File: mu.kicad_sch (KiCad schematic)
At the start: 69 parts, among them J1 JTAG-10 PIN, J4 2060-1452/998-404, J5 ESQ-110-X-X-D, U1 STM32F042F6P6, U10 TLV3603QDCKRQ1, U11 SN74LVC1G74DCUT, U12 LM4040AIM3-2.5/NOPB, U13 MCP4921-E/SN, U14 BMP390, U2 MAX5026EUT_T, U3 MICROFC-60035-SMT-TR1, U4 TLV70433DBVT, U5 W25Q128JVS, U6 OPA656NB/250, U8 LT3045xDD, U9 sn65hvd230

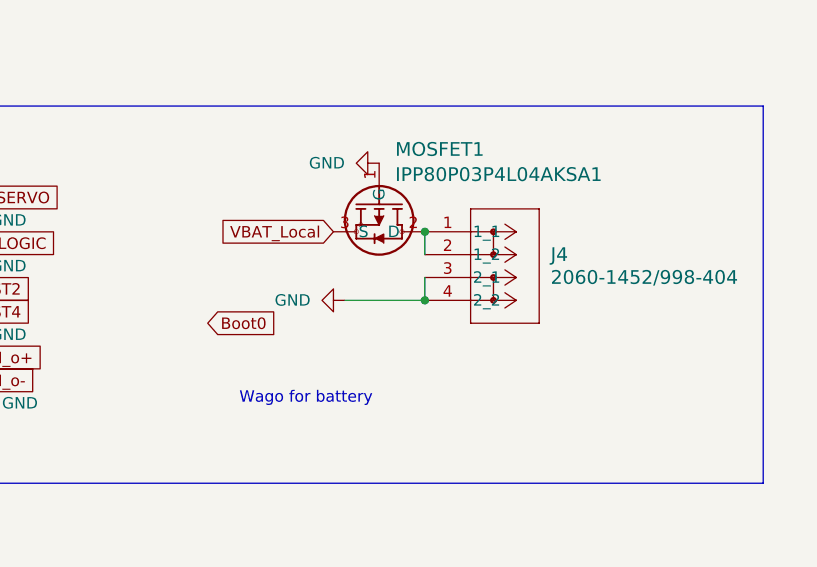
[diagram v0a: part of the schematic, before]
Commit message: xt30 added
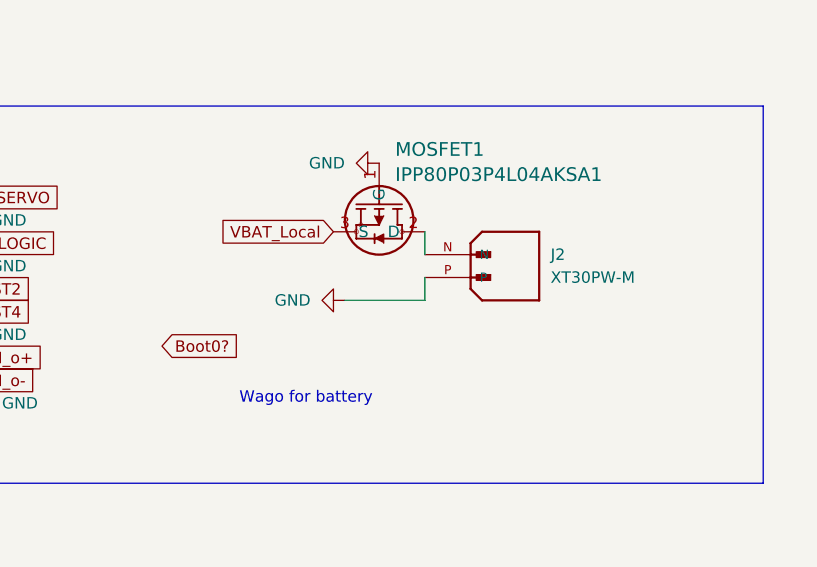
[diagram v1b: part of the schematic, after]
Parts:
- removed J4: 2060-1452/998-404, footprints:WAG, symbol Wago_2060-1452 998-404:2060-1452_998-404
- added J2: XT30PW-M, AMASS_XT30PW-M, symbol XT30PW-M:XT30PW-M
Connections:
- net GND: now also J2.P
- net at MOSFET1.2 (D): now also J2.N
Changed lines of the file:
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@@
 	)
 	(junction
-		(at 361.95 176.53)
-		(diameter 0)
-		(color 0 0 0 0)
-	)
-	(junction
 		(at 256.54 110.49)
 		(diameter 0)
@@
 	)
 	(junction
-		(at 361.95 184.15)
-		(diameter 0)
-		(color 0 0 0 0)
-	)
-	(junction
 		(at 213.36 215.9)
 		(diameter 0)
@@
 		)
 	)
-	(global_label "Boot0"
+	(global_label "Boot0?"
 		(shape input)
-		(at 337.82 186.69 0)
+		(at 332.74 189.23 0)
 		(fields_autoplaced yes)
 		(effects
@@
 		)
 		(property "Intersheetrefs" "${INTERSHEET_REFS}"
-			(at 346.3084 186.69 0)
+			(at 342.317 189.23 0)
 			(effects
 				(font
@@
 	)
 	(symbol
+		(lib_id "XT30PW-M:XT30PW-M")
+		(at 367.03 181.61 180)
+		(unit 1)
+		(exclude_from_sim no)
+		(in_bom yes)
+		(on_board yes)
+		(dnp no)
+		(fields_autoplaced yes)
+		(property "Reference" "J2"
+			(at 375.92 179.0699 0)
+			(effects
+				(font
+					(size 1.27 1.27)
+				)
+				(justify right)
+			)
+		)
+		(property "Value" "XT30PW-M"
+			(at 375.92 181.6099 0)
+			(effects
+				(font
+					(size 1.27 1.27)
+				)
+				(justify right)
+			)
+		)
+		(property "Footprint" "AMASS_XT30PW-M"
+			(at 367.03 181.61 0)
+			(effects
+				(font
+					(size 1.27 1.27)
+				)
+				(justify bottom)
+				(hide yes)
+			)
+		)
+		(property "Datasheet" ""
+			(at 367.03 181.61 0)
+			(effects
+				(font
+					(size 1.27 1.27)
+				)
+				(hide yes)
+			)
+		)
+		(property "Description" ""
+			(at 367.03 181.61 0)
+			(effects
+				(font
+					(size 1.27 1.27)
+				)
+				(hide yes)
+			)
+		)
+		(property "MF" "AMASS"
+			(at 367.03 181.61 0)
+			(effects
+				(font
+					(size 1.27 1.27)
+				)
+				(justify bottom)
+				(hide yes)
+			)
+		)
+		(property "MAXIMUM_PACKAGE_HEIGHT" "5 mm"
+			(at 367.03 181.61 0)
+			(effects
+				(font
+					(size 1.27 1.27)
+				)
+				(justify bottom)
+				(hide yes)
+			)
+		)
+		(property "Package" "None"
+			(at 367.03 181.61 0)
+			(effects
+				(font
+					(size 1.27 1.27)
+				)
+				(justify bottom)
+				(hide yes)
+			)
+		)
+		(property "Price" "None"
+			(at 367.03 181.61 0)
+			(effects
+				(font
+					(size 1.27 1.27)
+				)
+				(justify bottom)
+				(hide yes)
+			)
+		)
+		(property "Check_prices" "https://www.snapeda.com/parts/XT30PW-M/AMASS/view-part/?ref=eda"
+			(at 367.03 181.61 0)
+			(effects
+				(font
+					(size 1.27 1.27)
+				)
+				(justify bottom)
+				(hide yes)
+			)
+		)
+		(property "STANDARD" "Manufacturer Recommendations"
+			(at 367.03 181.61 0)
+			(effects
+				(font
+					(size 1.27 1.27)
+				)
+				(justify bottom)
+				(hide yes)
+			)
+		)
+		(property "PARTREV" "1.2"
+			(at 367.03 181.61 0)
+			(effects
+				(font
+					(size 1.27 1.27)
+				)
+				(justify bottom)
+				(hide yes)
+			)
+		)
+		(property "SnapEDA_Link" "https://www.snapeda.com/parts/XT30PW-M/AMASS/view-part/?ref=snap"
+			(at 367.03 181.61 0)
+			(effects
+				(font
+					(size 1.27 1.27)
+				)
+				(justify bottom)
+				(hide yes)
+			)
+		)
+		(property "MP" "XT30PW-M"
+			(at 367.03 181.61 0)
+			(effects
+				(font
+					(size 1.27 1.27)
+				)
+				(justify bottom)
+				(hide yes)
+			)
+		)
+		(property "Description_1" "Socket; DC supply; XT30; male; PIN: 2; on PCBs; THT; Colour: yellow"
+			(at 367.03 181.61 0)
+			(effects
+				(font
+					(size 1.27 1.27)
+				)
+				(justify bottom)
+				(hide yes)
+			)
+		)
+		(property "MANUFACTURER" "Amass"
+			(at 367.03 181.61 0)
+			(effects
+				(font
+					(size 1.27 1.27)
+				)
+				(justify bottom)
+				(hide yes)
+			)
+		)
+		(property "Availability" "In Stock"
+			(at 367.03 181.61 0)
+			(effects
+				(font
+					(size 1.27 1.27)
+				)
+				(justify bottom)
+				(hide yes)
+			)
+		)
+		(property "SNAPEDA_PN" "XT30PW-M"
+			(at 367.03 181.61 0)
+			(effects
+				(font
+					(size 1.27 1.27)
+				)
+				(justify bottom)
+				(hide yes)
+			)
+		)
+		(pin "N"
+		)
+		(pin "P"
+		)
+		(instances
+			(project ""
+				(path "/0020f91a-50ae-478d-8303-55d8991d2d34"
+					(reference "J2")
+					(unit 1)
+				)
+			)
+		)
+	)
+	(symbol
 		(lib_id "power:GND")
 		(at 208.28 191.77 0)
@@
 					(unit 1)
 				)
-			)
-		)
-	)
-	(symbol
-		(lib_id "Wago_2060-1452 998-404:2060-1452_998-404")
-		(at 361.95 176.53 0)
-		(unit 1)
-		(exclude_from_sim no)
-		(in_bom yes)
-		(on_board yes)
-		(dnp no)
-		(fields_autoplaced yes)
-		(property "Reference" "J4"
-			(at 375.92 179.0699 0)
-			(effects
-				(font
-					(size 1.524 1.524)
-				)
-				(justify left)
-			)
-		)
-		(property "Value" "2060-1452/998-404"
-			(at 375.92 181.6099 0)
-			(effects
-				(font
-					(size 1.524 1.524)
-				)
-				(justify left)
-			)
-		)
-		(property "Footprint" "footprints:WAG"
-			(at 361.95 176.53 0)
-			(effects
-				(font
-					(size 1.27 1.27)
-					(italic yes)
-				)
-				(hide yes)
-			)
-		)
-		(property "Datasheet" "2060-1452/998-404"
-			(at 361.95 176.53 0)
-			(effects
-				(font
-					(size 1.27 1.27)
-					(italic yes)
-				)
-				(hide yes)
-			)
-		)
-		(property "Description" ""
-			(at 361.95 176.53 0)
-			(effects
-				(font
-					(size 1.27 1.27)
-				)
-				(hide yes)
-			)
-		)
-		(pin "1"
-		)
-		(pin "4"
-		)
-		(pin "3"
-		)
-		(pin "2"
-		)
-		(instances
-			(project "mu"
-				(path "/0020f91a-50ae-478d-8303-55d8991d2d34"
-					(reference "J4")
-					(unit 1)
-				)

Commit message: fixed the connector
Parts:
- removed C32: 100nF, Resistor_SMD:R_0402_1005Metric, symbol Device:C
- removed R16: 2.49KΩ 0.1%, Resistor_SMD:R_0402_1005Metric, symbol Device:R
- removed U12: LM4040AIM3-2.5/NOPB, DBZ3, symbol LM4040AIM3-2-5-NOPB:LM4040AIM3-2.5_NOPB
- added J3: U.FL-R-SMT-1_10_, HRS_U.FL-R-SMT-1_10_, symbol U.FL-R-SMT-1_10_:U.FL-R-SMT-1_10_
- added J4: ESQ-110-X-X-D, SAMTEC_ESQ-110-14-G-D, symbol ESQ-110-X-X-D:ESQ-110-X-X-D
- added R7: 0Ω, Resistor_SMD:R_0402_1005Metric, symbol Device:R
- added R8: 50Ω 0.1%, Resistor_SMD:R_0402_1005Metric, symbol Device:R
- R1: value 220K -> 210K
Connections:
- net 2.5V_Ref is gone; now on net GND: R3.1, Rg1.2, U3.1
- net 5V_LOGIC: now also J4.05, J4.06
- net 5v_SERVO: now also J4.01, J4.02; no longer J5.01, J5.02
- net CAN_o+: now also J4.16
- net CAN_o-: now also J4.18
- net GND: now also J2.N, J3.1, J3.3, J4.03, J4.04, J4.07, J4.08, J4.14, J4.19, J4.20; no longer J2.P
- net NRST: now also J4.17
- net SWDIO: now also J4.15
- net at MOSFET1.2 (D): now also J2.P; no longer J2.N
- net at RF1.2, U10.3 (IN+), U6.1 (OUTPUT): now also R7.1
- net NRST1: no longer names the net of J5.09
- net NRST2: no longer names the net of J5.10
- net NRST3: no longer names the net of J5.11
- net NRST4: no longer names the net of J5.12
- net NRST5: no longer names the net of J5.13
- new net: R7.2, R8.2
- new net: J3.2, R8.1
- new net SWCLK1: J4.09
- new net SWCLK2: J4.10
- new net SWCLK3: J4.11
- new net SWCLK4: J4.12
- new net SWCLK5: J4.13
- no-connect marks 15 -> 21
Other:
- note added: "+27.5V"
- note added: "Accounts for potential -1.29v vibas drift from 20C to -40"
- note added: "This HV line is used to provide the reverse bias to the SiPM."
- note added: "XT30 for battery"
- note added: "this is going up 9km, is the bias voltage ok? yes."
- note removed: "28.75V"
- note removed: "Takes the 5V line and creates a 2.5V reference"
- note removed: "This HV line is used to provide the reverse bias to the SiPM. The SiPM sees 30V difference, as virtual ground is 2.5V"
- note removed: "Virtual Ground Reference"
- note removed: "Wago for battery"
- note removed: "this is going up 9km, is the bias voltage ok?"
- note removed: "to detect dips when current pulses hit opp amp, using a shunt regulator"
- moved on the sheet: C5, C6, J1, J2, R3, U6

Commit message: fixed the connector
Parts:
- removed R5: 10K, Resistor_SMD:R_0402_1005Metric, symbol Device:R
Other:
- moved on the sheet: C13
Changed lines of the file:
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@@
 	)
 	(junction
-		(at 113.03 190.5)
-		(diameter 0)
-		(color 0 0 0 0)
-	)
-	(junction
 		(at 33.02 132.08)
 		(diameter 0)
@@
 	)
 	(junction
-		(at 113.03 194.31)
-		(diameter 0)
-		(color 0 0 0 0)
-	)
-	(junction
 		(at 99.06 62.23)
 		(diameter 0)
@@
 	(wire
 		(pts
-			(xy 113.03 201.93) (xy 113.03 203.2)
-		)
-		(stroke
-			(width 0)
-			(type default)
-		)
-	)
-	(wire
-		(pts
 			(xy 194.31 128.27) (xy 194.31 129.54)
 		)
@@
 	(wire
 		(pts
-			(xy 119.38 181.61) (xy 120.65 181.61)
+			(xy 113.03 190.5) (xy 113.03 193.04)
 		)
 		(stroke
@@
 	(wire
 		(pts
-			(xy 113.03 194.31) (xy 118.11 194.31)
+			(xy 119.38 181.61) (xy 120.65 181.61)
 		)
 		(stroke
@@
 	(wire
 		(pts
-			(xy 113.03 189.23) (xy 113.03 190.5)
-		)
-		(stroke
-			(width 0)
-			(type default)
-		)
-	)
-	(wire
-		(pts
 			(xy 72.39 119.38) (xy 81.28 119.38)
 		)
@@
 	(wire
 		(pts
-			(xy 113.03 190.5) (xy 113.03 194.31)
-		)
-		(stroke
-			(width 0)
-			(type default)
-		)
-	)
-	(wire
-		(pts
 			(xy 231.14 176.53) (xy 234.95 176.53)
 		)
@@
 	(global_label "NRST"
 		(shape input)
-		(at 113.03 189.23 0)
+		(at 113.03 190.5 0)
 		(fields_autoplaced yes)
 		(effects
@@
 		)
 		(property "Intersheetrefs" "${INTERSHEET_REFS}"
-			(at 120.7928 189.23 0)
+			(at 120.7928 190.5 0)
 			(effects
 				(font
@@
 		)
 	)
-	(global_label "3.3V_Dig"
-		(shape input)
-		(at 125.73 194.31 0)
-		(fields_autoplaced yes)
-		(effects
-			(font
-				(size 1.27 1.27)
-			)
-			(justify left)
-		)
-		(property "Intersheetrefs" "${INTERSHEET_REFS}"
-			(at 136.819 194.31 0)
-			(effects
-				(font
-					(size 1.27 1.27)
-				)
-				(justify left)
-				(hide yes)
-			)
-		)
-	)
 	(global_label "HV"
 		(shape input)
@@
 	(symbol
 		(lib_id "Device:C")
-		(at 113.03 198.12 0)
+		(at 113.03 196.85 0)
 		(unit 1)
 		(exclude_from_sim no)
@@
 		(dnp no)
 		(property "Reference" "C13"
-			(at 115.062 195.834 0)
+			(at 115.062 194.564 0)
 			(effects
 				(font
@@
 		)
 		(property "Value" "100nF"
-			(at 114.554 202.184 90)
+			(at 115.57 200.914 90)
 			(effects
 				(font
@@
 		)
 		(property "Footprint" "Capacitor_SMD:C_0402_1005Metric"
-			(at 113.9952 201.93 0)
+			(at 113.9952 200.66 0)
 			(effects
 				(font
@@
 		)
 		(property "Datasheet" "~"
-			(at 113.03 198.12 0)
+			(at 113.03 196.85 0)
 			(effects
 				(font
@@
 		)
 		(property "Description" "Unpolarized capacitor"
-			(at 113.03 198.12 0)
+			(at 113.03 196.85 0)
 			(effects
 				(font
@@
 	(symbol
 		(lib_id "power:GND")
-		(at 113.03 203.2 0)
+		(at 113.03 200.66 0)
 		(unit 1)
 		(exclude_from_sim no)
@@
 		(on_board yes)
 		(dnp no)
-		(fields_autoplaced yes)
 		(property "Reference" "#PWR013"
-			(at 113.03 209.55 0)
+			(at 113.03 207.01 0)
 			(effects
 				(font
@@
 		)
 		(property "Value" "GND"
-			(at 113.0301 207.01 90)
+			(at 114.554 204.47 0)
 			(effects
 				(font
@@
 		)
 		(property "Footprint" ""
-			(at 113.03 203.2 0)
+			(at 113.03 200.66 0)
 			(effects
 				(font
@@
 		)
 		(property "Datasheet" ""
-			(at 113.03 203.2 0)
+			(at 113.03 200.66 0)
 			(effects
 				(font
@@
 		)
 		(property "Description" "Power symbol creates a global label with name \"GND\" , ground"
-			(at 113.03 203.2 0)
+			(at 113.03 200.66 0)
 			(effects
 				(font
@@
 					(unit 1)
 				)
-			)
-		)
-	)
-	(symbol
-		(lib_id "Device:R")
-		(at 121.92 194.31 90)
-		(unit 1)
-		(exclude_from_sim no)
-		(in_bom yes)
-		(on_board yes)
-		(dnp no)
-		(property "Reference" "R5"
-			(at 119.38 192.278 90)
-			(effects
-				(font
-					(size 1.27 1.27)
-				)
-				(justify right)
-			)
-		)
-		(property "Value" "10K"
-			(at 119.888 194.31 90)
-			(effects
-				(font
-					(size 1.27 1.27)
-				)
-				(justify right)
-			)
-		)
-		(property "Footprint" "Resistor_SMD:R_0402_1005Metric"
-			(at 121.92 196.088 90)
-			(effects
-				(font
-					(size 1.27 1.27)
-				)
-				(hide yes)
-			)
-		)
-		(property "Datasheet" "~"
-			(at 121.92 194.31 0)
-			(effects
-				(font
-					(size 1.27 1.27)
-				)
-				(hide yes)
-			)
-		)
-		(property "Description" "Resistor"
-			(at 121.92 194.31 0)
-			(effects
-				(font
-					(size 1.27 1.27)
-				)
-				(hide yes)
-			)
-		)
-		(pin "1"
-		)
-		(pin "2"
-		)
-		(instances
-			(project "mu"
-				(path "/0020f91a-50ae-478d-8303-55d8991d2d34"
-					(reference "R5")
-					(unit 1)
-				)

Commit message: major revisions
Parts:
- added C32, C33: 8pF, Capacitor_SMD:C_0402_1005Metric, symbol Device:C
- added XTAL1: NX3225GD-8MHZ-STD-CRA-3, XTAL_NX3225GD-8MHZ-STD-CRA-3_NDK, symbol STDCRA38M:NX3225GD-8MHZ-STD-CRA-3
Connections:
- net GND: now also C32.1, C33.2
- net at U1.2 (PF0-OSC_IN): now also C33.1, XTAL1.2
- net at U1.3 (PF1-OSC_OUT): now also C32.2, XTAL1.1
- no-connect marks 21 -> 19

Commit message: drc pass
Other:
- note added: "interboard connector standard (not placed, just for reference)"
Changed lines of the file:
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@@
 		)
 	)
-	(text "interboard connector"
+	(text "interboard connector standard\n(not placed, just for reference)"
 		(exclude_from_sim no)
 		(at 369.57 248.412 0)

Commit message: 3d model  made
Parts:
- added J6: Conn_01x05_Pin, symbol Connector:Conn_01x05_Pin
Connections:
- net SWCLK1 is gone; now on net GND: J4.09
- net SWCLK2 is gone; now on net GND: J4.10
- net SWCLK3 is gone; now on net 5V_LOGIC: J4.11
- net SWCLK4 is gone; now on net 5V_LOGIC: J4.12
- net 3.3V_Dig: now also J6.2 (Pin_2)
- net 5V_LOGIC: no longer J4.05, J4.06
- net 5v_SERVO: now also J4.03, J4.04, J4.05, J4.06, J4.07, J4.08; no longer J4.01, J4.02
- net GND: now also J4.01, J4.02, J6.1 (Pin_1); no longer J4.03, J4.04, J4.07, J4.08
- net NRST: now also J6.3 (Pin_3); no longer J4.17
- net SWCLK: now also J6.5 (Pin_5)
- net SWDIO: now also J6.4 (Pin_4); no longer J4.15
- net SWCLK5: no longer names the net of J4.13

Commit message: refdes, test points, better connector
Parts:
- removed J1: JTAG-10 PIN, Connector_IDC:IDC-Header_2x05_P2.54mm_Vertical, symbol Connector_Generic_MountingPin:Conn_01x10_MountingPin
- removed J6: Conn_01x05_Pin, symbol Connector:Conn_01x05_Pin
- removed MOSFET1: IPP80P03P4L04AKSA1, PG-TO220-3-1_INF, symbol IPP80P03P4L04AKSA1:IPP80P03P4L04AKSA1
- added J1, J10, J11, J12, J13, J6, J8, J9: S2761-46R, HARWIN_S2761-46R, symbol S2761-46R:S2761-46R
- added J7: 5023860570, MOLEX_5023860570, symbol 5023860570:5023860570
- added Q1: IPD90P04P4L04ATMA1, footprints:PG-TO252-3-313_INF-L, symbol IPD90P04P4L04ATMA1:IPD90P04P4L04ATMA1
- U6: value OPA656NB/250 -> OPA656NB/250 or OPA814
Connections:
- net 3.3V_Dig: now also J1.1, J7.4
- net 5V: now also J6.1
- net 5V_LOGIC: now also J5.11, J5.12; no longer J5.05, J5.06
- net 5v_SERVO: now also J5.03, J5.04, J5.05, J5.06, J5.07, J5.08
- net CAN_o+: now also J13.1
- net CAN_o-: now also J12.1
- net GND: now also J4.13, J4.15, J4.17, J5.01, J5.02, J5.09, J5.10, J5.13, J5.15, J5.17, J7.5, J7.S1 (SHIELD1), J7.S2 (SHIELD2), J8.1, Q1.1 (G); no longer J5.03, J5.04, J5.07, J5.08
- net HV: now also J9.1
- net Latch_Out: now also J10.1
- net Latch_Rst: now also J11.1
- net NRST: now also J7.3
- net SWCLK: now also J7.1
- net SWDIO: now also J7.2
- net VBAT_Local: now also Q1.3 (S)
- net at J2.P: now also Q1.2 (D)
- no-connect marks 19 -> 6
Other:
- note removed: "Connector_IDC:IDC-Header_2x05_P2.54mm_Vertical"

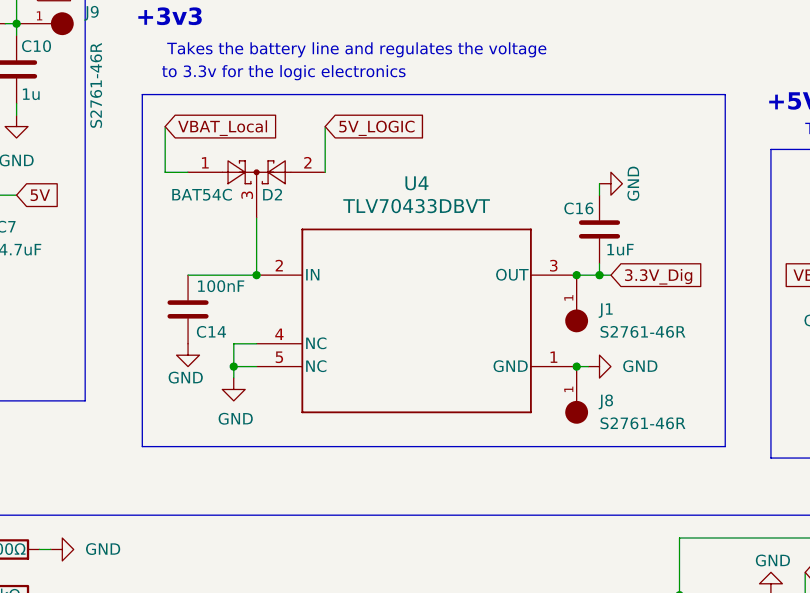
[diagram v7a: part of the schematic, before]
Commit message: power subschematic done
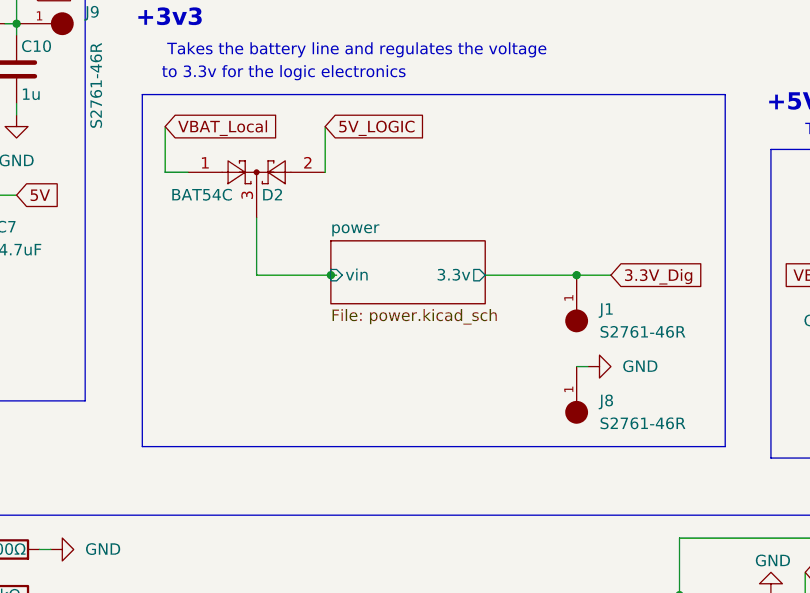
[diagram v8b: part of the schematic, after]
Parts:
- removed C14: 100nF, Resistor_SMD:R_0402_1005Metric, symbol Device:C
- removed C16: 1uF, Capacitor_SMD:C_0402_1005Metric, symbol Device:C
- removed U4: TLV70433DBVT, DBV0005A_N, symbol TLV70433DBVT:TLV70433DBVT
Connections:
- net power/vin: now reaches D2.3
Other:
- added sheet power (power.kicad_sch)
